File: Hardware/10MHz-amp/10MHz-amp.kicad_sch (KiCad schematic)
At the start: 27 parts, among them J1 Conn_Coaxial, J2 Jack-DC, J3 Conn_Coaxial, Q1 PMOS, SW1 SW_SP5T_NR01105, SW2 SW_SPDT, U1 THS3491xDDA

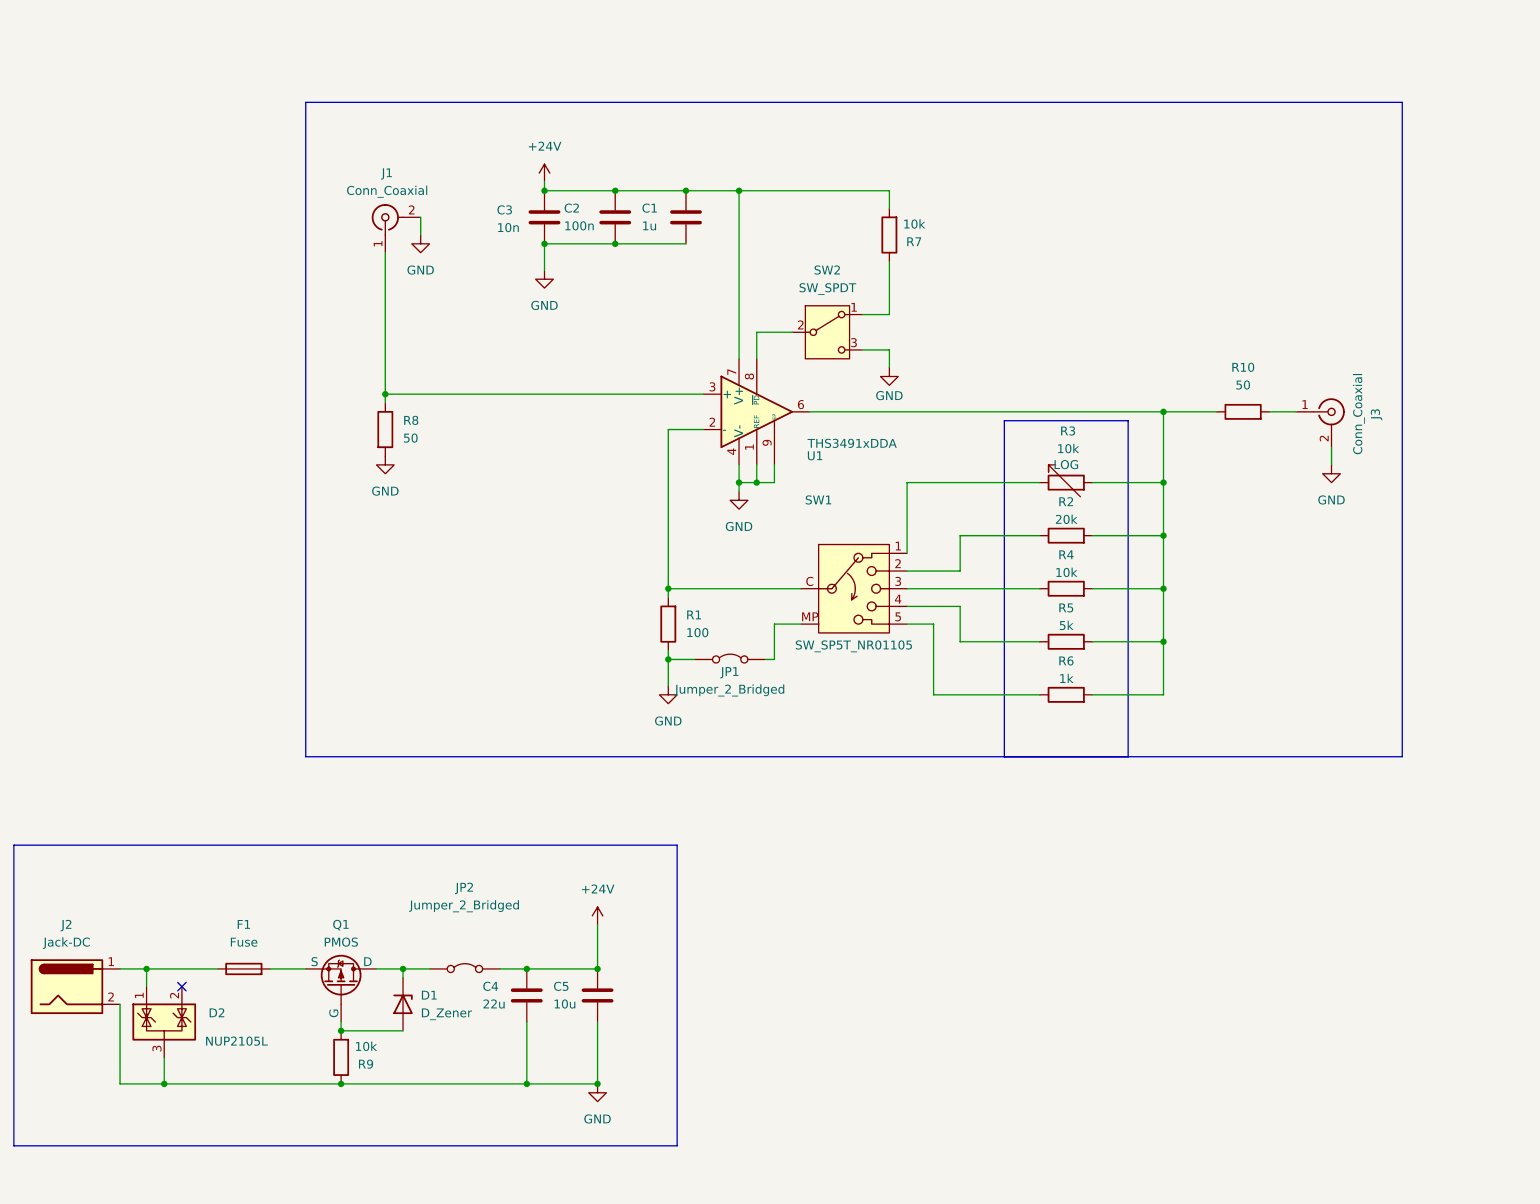
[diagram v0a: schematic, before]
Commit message: added housing
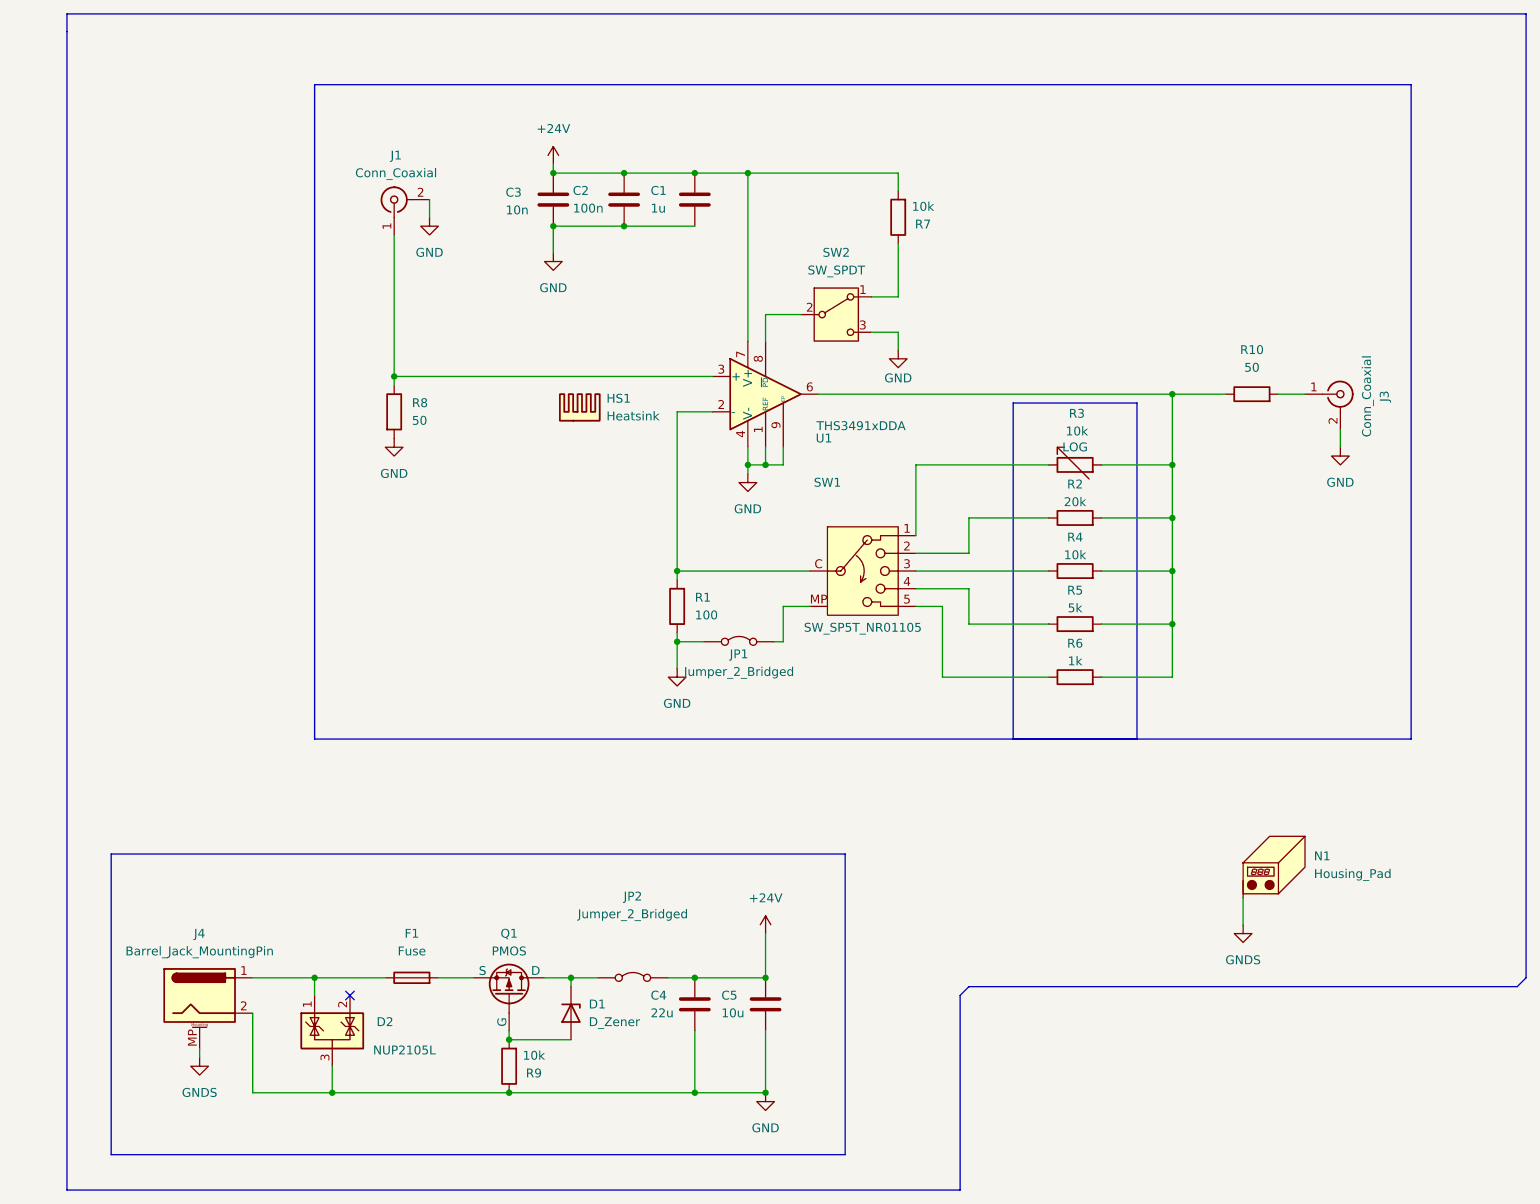
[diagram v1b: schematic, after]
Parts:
- removed J2: Jack-DC, symbol Connector:Jack-DC
- added HS1: Heatsink, symbol Mechanical:Heatsink
- added J4: Barrel_Jack_MountingPin, symbol Connector:Barrel_Jack_MountingPin
- added N1: Housing_Pad, symbol Mechanical:Housing_Pad
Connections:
- net GND: now also J4.2
- net at D2.1 (K), F1.1: now also J4.1
- new net GNDS: J4.MP (MountPin), N1.1 (PAD)
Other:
- moved on the sheet: C1, C2, C3, C4, C5, D1, D2, F1, J1, J3, JP1, JP2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

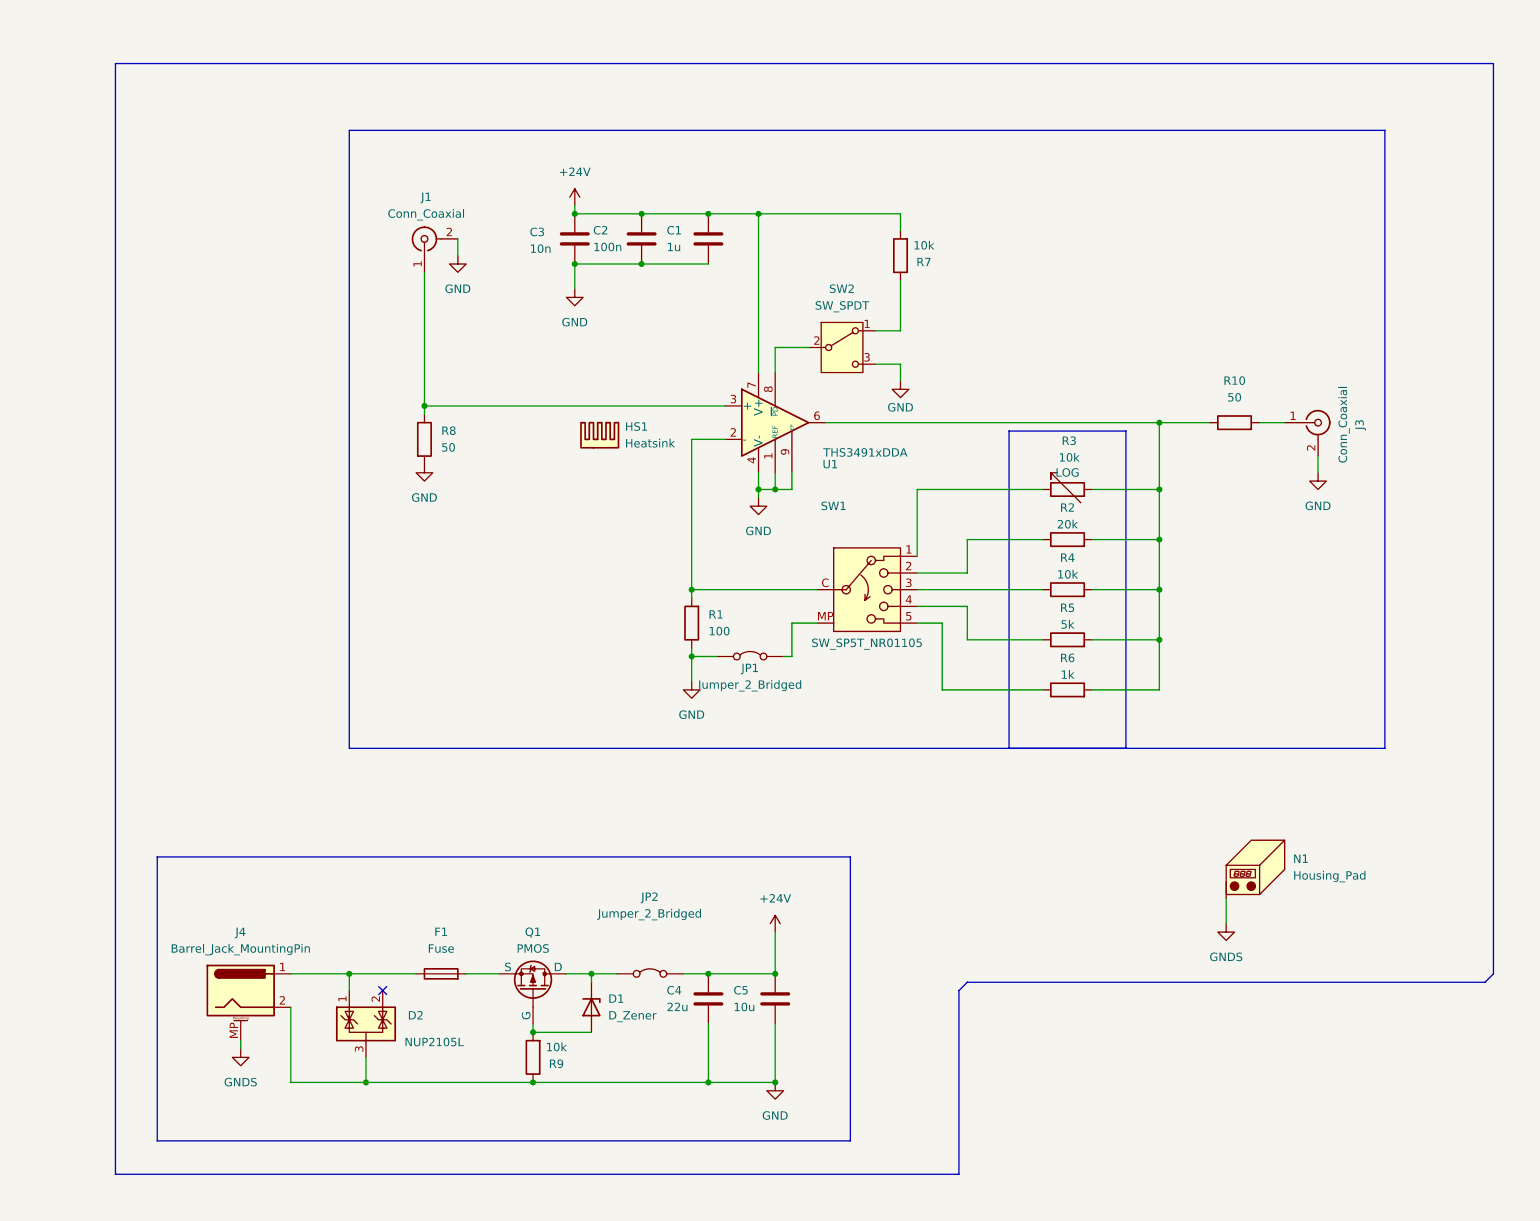
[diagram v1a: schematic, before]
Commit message: swapped to using relays instead of the rotor switch
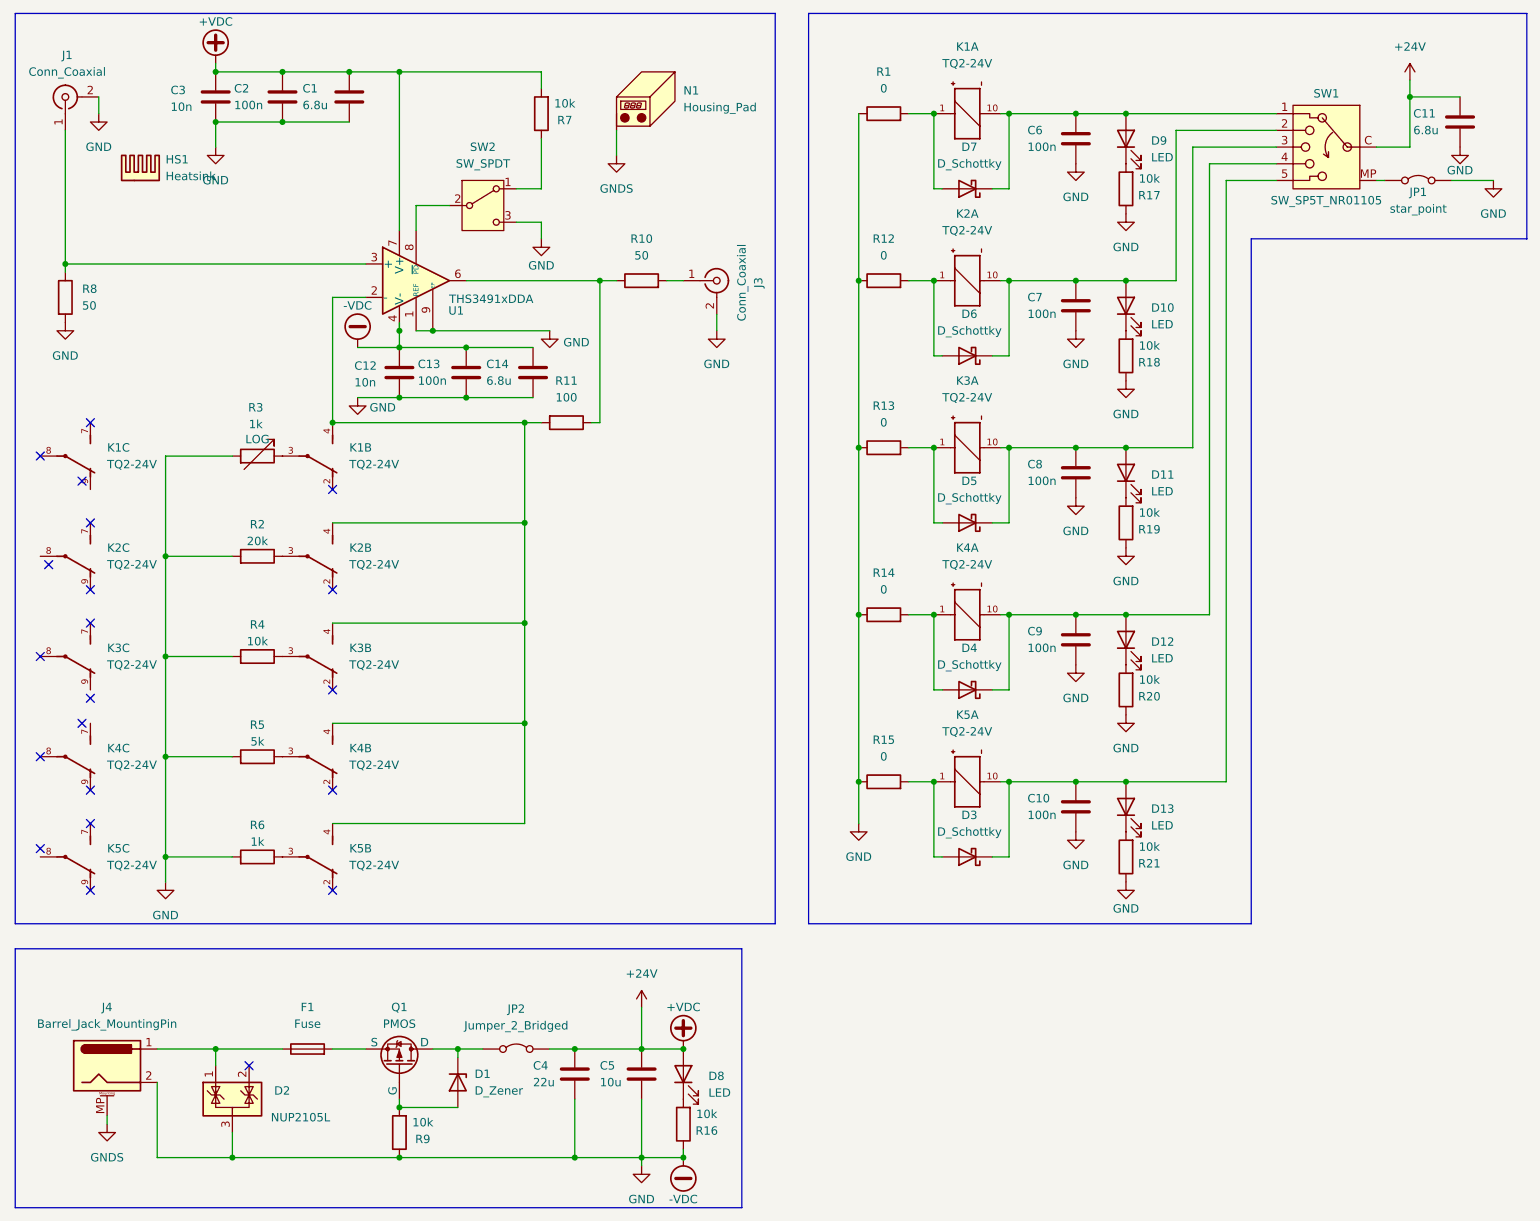
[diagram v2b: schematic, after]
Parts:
- added C10, C13, C6, C7, C8, C9: 100n, symbol Device:C
- added C11, C14: 6.8u, symbol Device:C
- added C12: 10n, symbol Device:C
- added D10, D11, D12, D13, D8, D9: LED, symbol Device:LED
- added D3, D4, D5, D6, D7: D_Schottky, symbol Device:D_Schottky
- added K1, K2, K3, K4, K5: TQ2-24V, TQ2-5V:TQ2, symbol TQ2-5V:TQ2-5V
- added R11: 100, symbol Device:R
- added R12, R13, R14, R15: 0, symbol Device:R
- added R16, R17, R18, R19, R20, R21: 10k, symbol Device:R
- C1: value 1u -> 6.8u
- JP1: value Jumper_2_Bridged -> star_point
- R1: value 100 -> 0
- R3: value 10k -> 1k
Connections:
- net GND is gone; now on net -VDC: C1.2, C2.2, C3.2, C4.2, C5.2, D2.3 (A), J1.2 (Ext), J3.2 (Ext), J4.2, JP1.1 (A), R1.1, R8.2, R9.1, SW2.3 (C), U1.1 (REF), U1.4 (V-), U1.9 (EP)
- net +24V: now also SW1.C (Common), C11.1, D8.2 (A)
- net at R5.1: now also K4.3; no longer SW1.4
- net -VDC: now reaches R2.2, R3.2, R4.2, R5.2, R6.2
- net -VDC: now also C10.2, C11.2, C12.1, C12.2, C13.1, C13.2, C14.1, C14.2, C6.2, C7.2, C8.2, C9.2, R12.1, R13.1, R14.1, R15.1, R16.1, R17.1, R18.1, R19.1, R20.1, R21.1; no longer R10.1, U1.6
- net at SW1.5: now also C10.1, D13.2 (A), D3.1 (K), K5.10; no longer R6.1
- net at R2.1: now also K2.3; no longer SW1.2
- net at SW1.1: now also C6.1, D7.1 (K), D9.2 (A), K1.10; no longer R3.1
- net at SW1.3: now also C8.1, D11.2 (A), D5.1 (K), K3.10; no longer R4.1
- new net: D9.1 (K), R17.2
- new net: D4.2 (A), K4.1, R14.2
- new net: C9.1, D12.2 (A), D4.1 (K), K4.10, SW1.4
- new net: K5.3, R6.1
- new net: D7.2 (A), K1.1, R1.2
- new net: D8.1 (K), R16.2
- new net: K1.4, K2.4, K3.4, K4.4, K5.4, R11.2, U1.2 (-)
- new net: C7.1, D10.2 (A), D6.1 (K), K2.10, SW1.2
- new net: D11.1 (K), R19.2
- new net: K1.3, R3.1
- new net: K3.3, R4.1
- new net: D3.2 (A), K5.1, R15.2
- new net: D6.2 (A), K2.1, R12.2
- new net: D13.1 (K), R21.2
- new net: D12.1 (K), R20.2
- new net: R10.1, R11.1, U1.6
- new net: D5.2 (A), K3.1, R13.2
- new net: D10.1 (K), R18.2
- no-connect marks 1 -> 21
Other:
- moved on the sheet: C1, C2, C3, C4, C5, D1, D2, F1, HS1, J1, J3, J4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
